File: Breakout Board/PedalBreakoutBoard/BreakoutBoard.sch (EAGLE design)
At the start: 40 parts

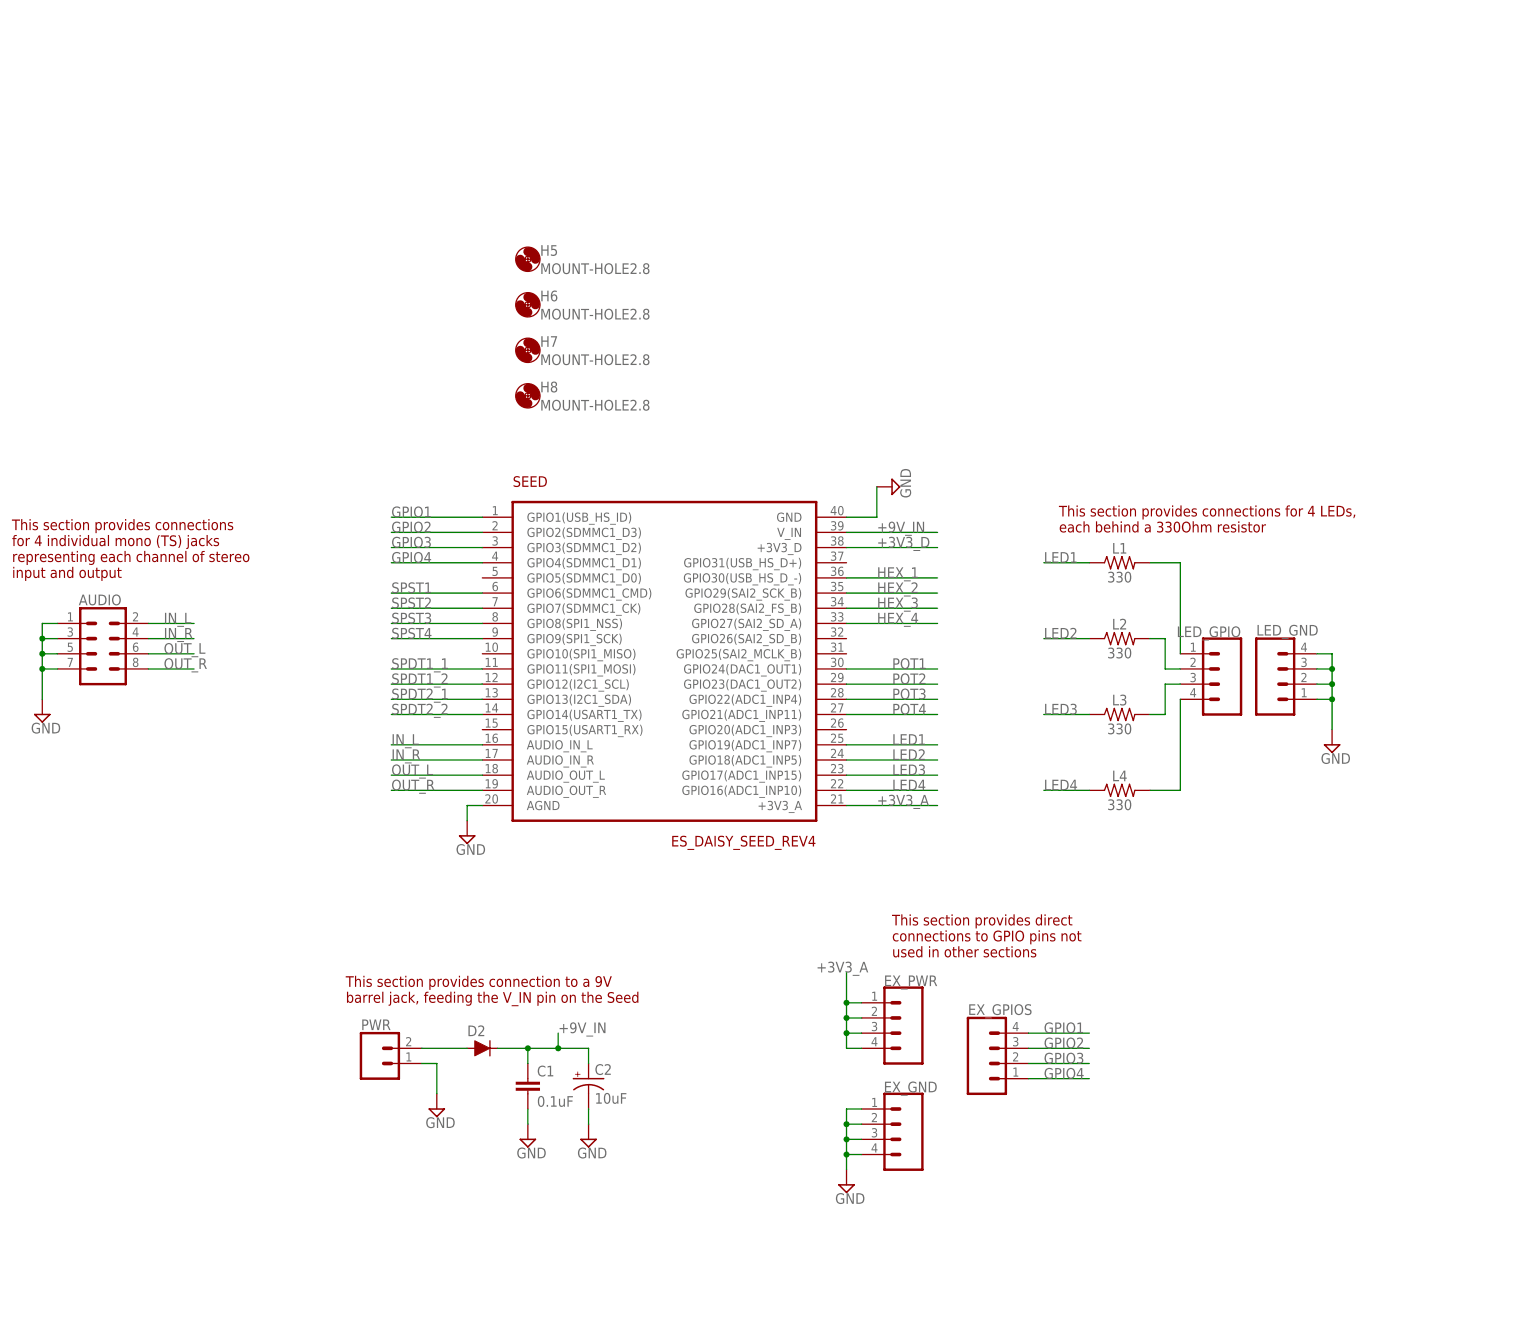
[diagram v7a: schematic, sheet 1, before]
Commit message: DP-33 - Added power section
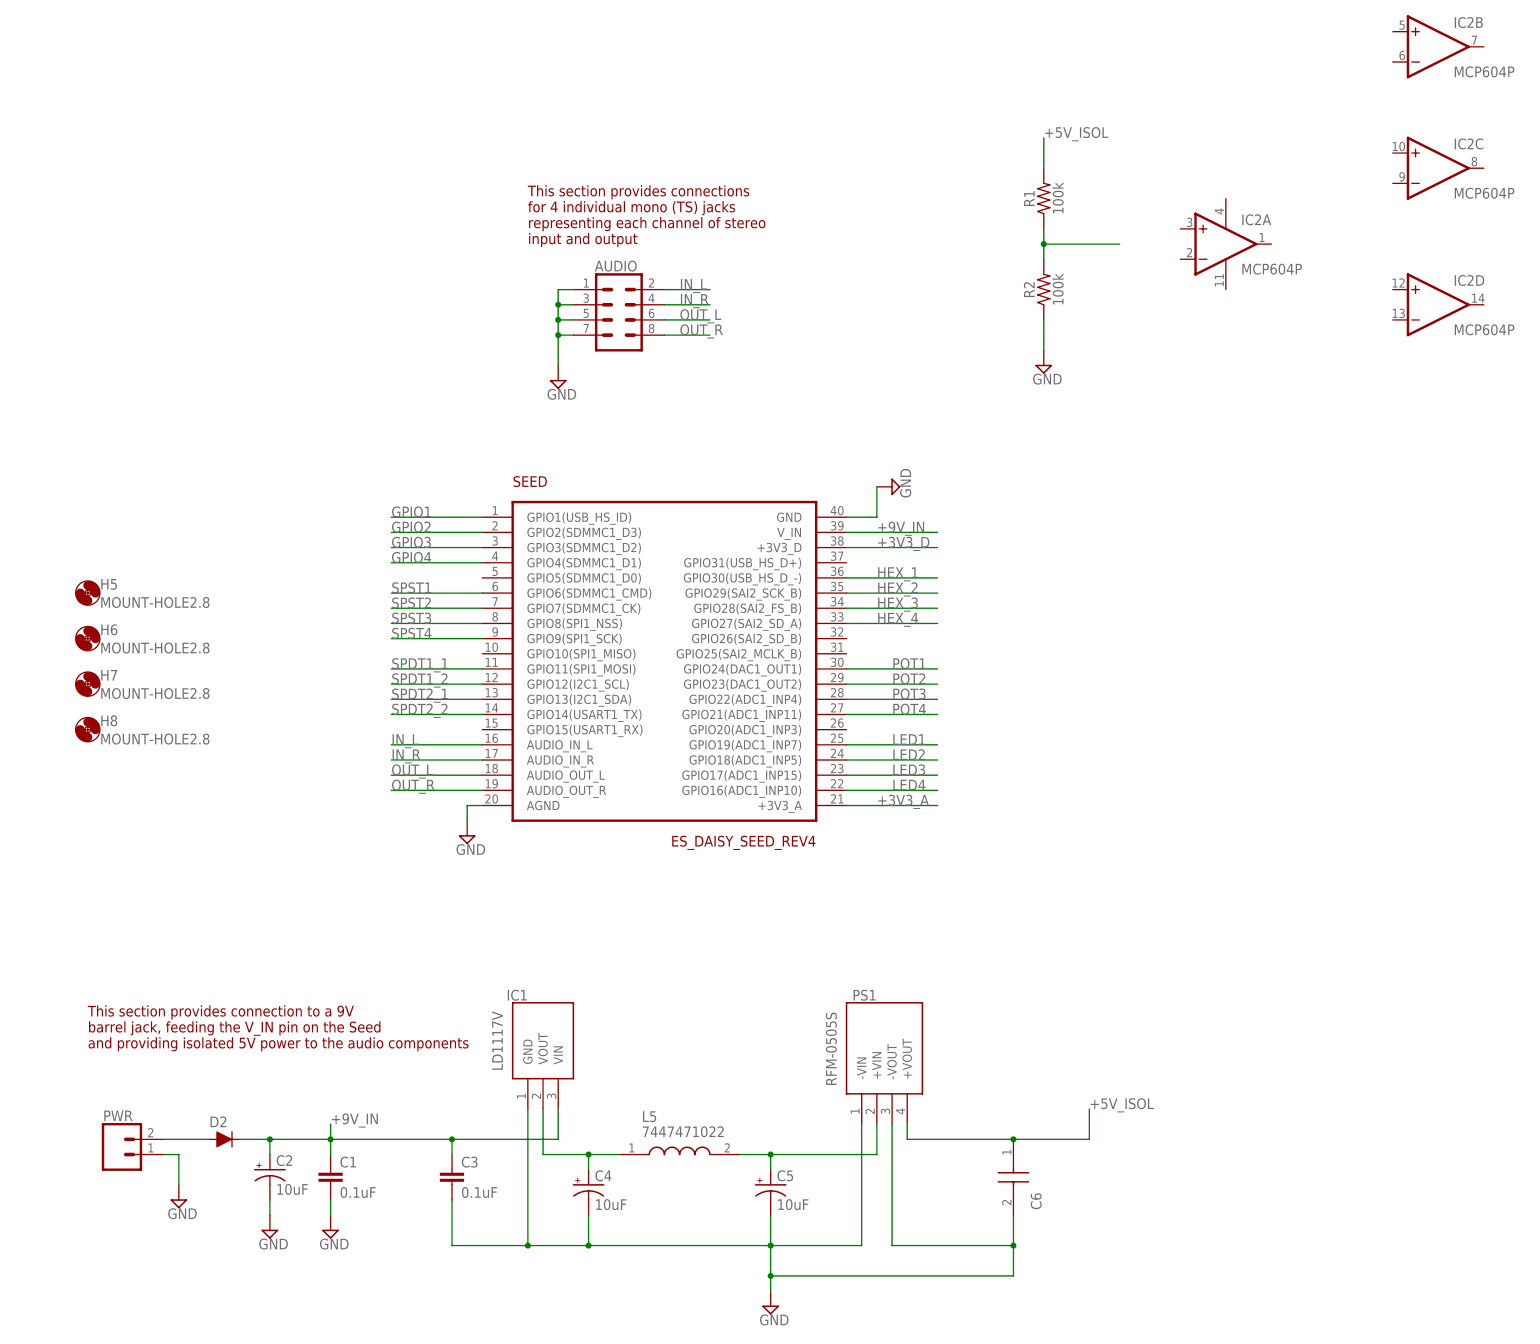
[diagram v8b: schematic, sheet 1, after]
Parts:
- added C3: 0.1uF, SparkFun-Capacitors:0.1UF-KIT-EZ-50V-20%
- added C4, C5: 10uF, SparkFun-Capacitors:10UF-POLAR-RADIAL-2.5MM-25V-20%
- added C6: RDEC71H226MWK1H03B, SamacSys_Parts:RDEC71H226MWK1H03B
- added IC1: LD1117V, SamacSys_Parts:LD1117V
- added IC2: MCP604P, linear:MCP604P
- added L5: 7447471022, SamacSys_Parts:7447471022
- added PS1: RFM-0505S, SamacSys_Parts:RFM-0505S
- added R1, R2: 100k, SparkFun-Resistors:100KOHM-HORIZ-1/4W-5%
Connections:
- new net +5V_ISOL: C6.1, PS1.+VOUT, R1.2
- new net N$6: R1.1, R2.2
- new net N$7: C5.+, L5.2, PS1.+VIN
- new net N$8: C4.+, IC1.VOUT, L5.1
- net +9V_IN: now also C3.1, IC1.VIN
- net GND: now also C3.2, C4.-, C5.-, C6.2, IC1.GND, PS1.-VIN, PS1.-VOUT, R2.1
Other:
- note added: "This section provides connection to a 9V barrel jack, feeding the V_IN pin on the Seed and providing isolated 5V power to the audio components"
- note removed: "This section provides connection to a 9V barrel jack, feeding the V_IN pin on the Seed"
- moved on the sheet: AUDIO, C1, C2, D2, H5, H6, H7, H8, PWR
